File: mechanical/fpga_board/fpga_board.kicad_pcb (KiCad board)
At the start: 4 copper layers, 92 x 92 mm, 52 parts, among them J1 Conn_02x17_Odd_Even, J10 Conn_01x01, J2 Conn_02x17_Odd_Even, J3 Conn_02x17_Odd_Even, J4 Conn_02x17_Odd_Even, J5 Conn_02x17_Odd_Even, J6 jtag, J7 Conn_02x03_Odd_Even, J8 Conn_02x12_Odd_Even, J9 Conn_01x01, U1 XC6SLX16-FTG256, U2 SiT1602, U3 MIC5504-3.3YM5, U4 MIC5504-1.2YM5

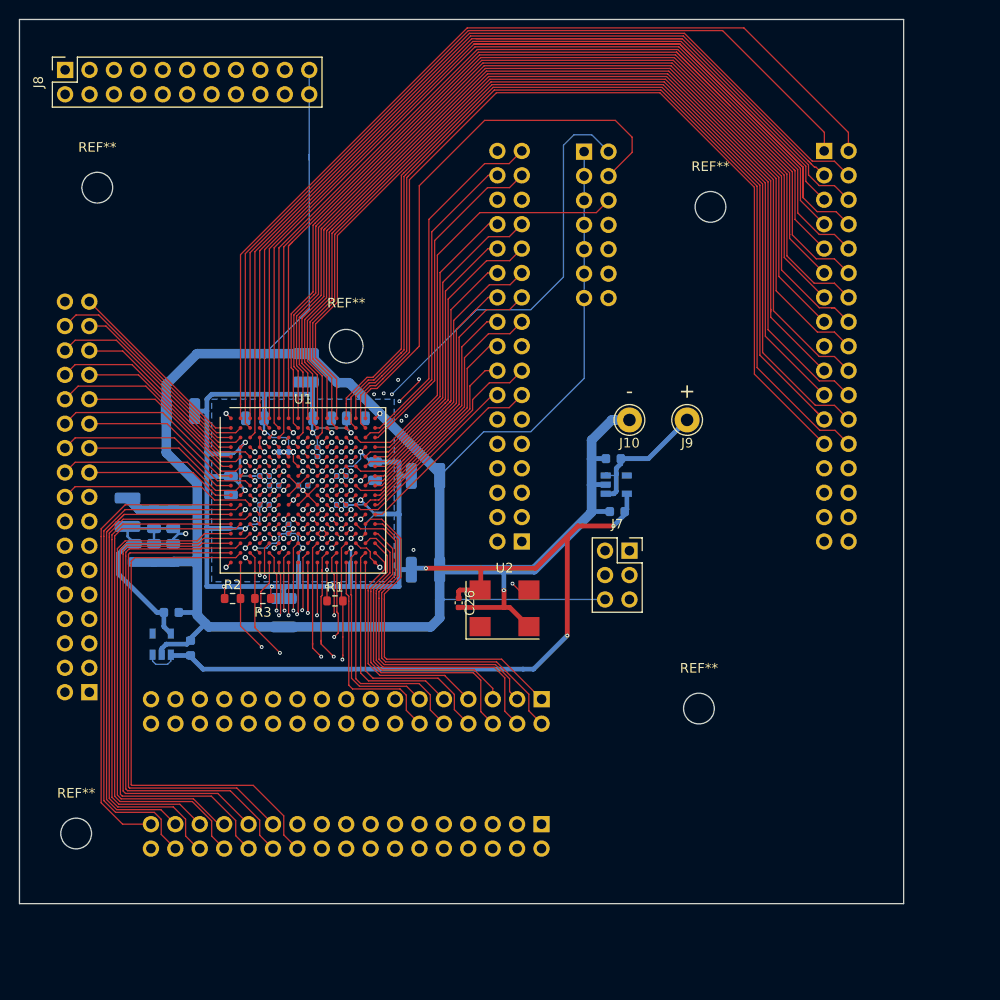
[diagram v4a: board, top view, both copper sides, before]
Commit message: Shortened some traces
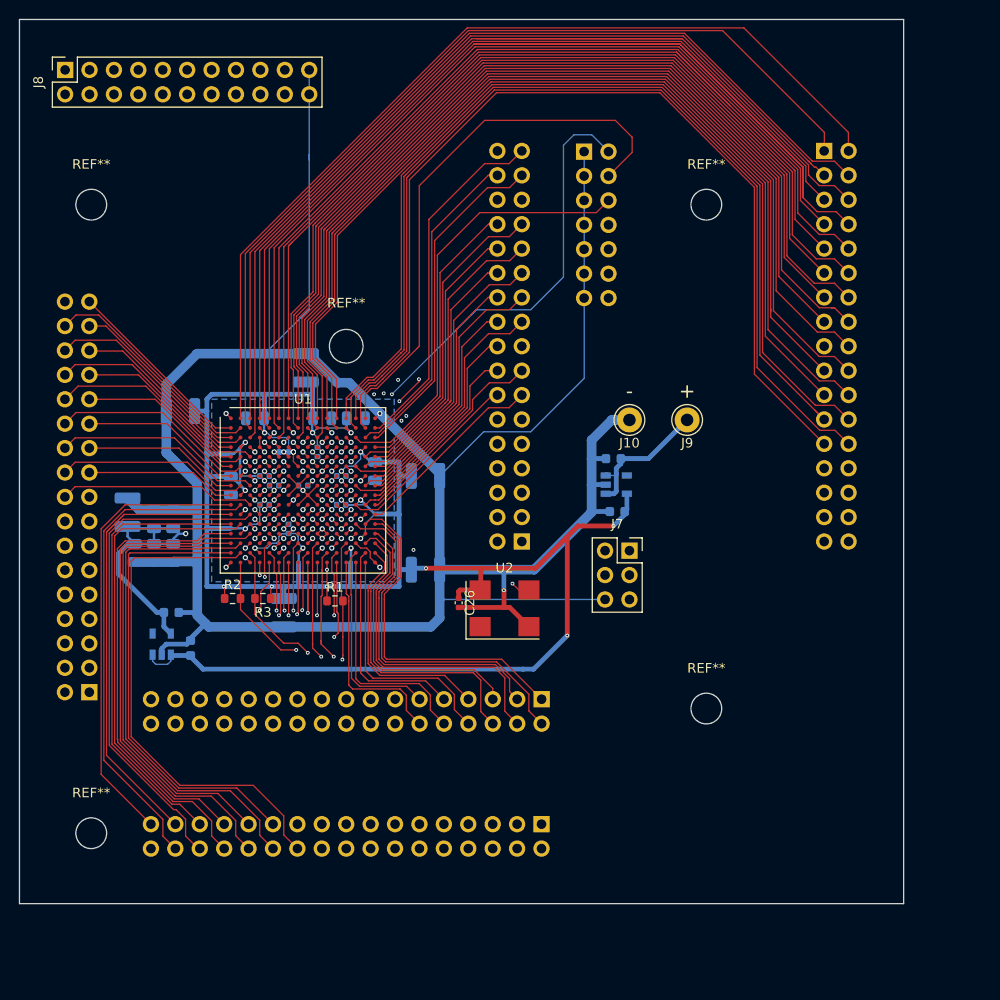
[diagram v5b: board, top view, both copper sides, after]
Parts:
- moved REF** 1.88 mm to (246.0, 174.0)
- moved REF** 1.57 mm to (246.0, 239.4)
- moved REF** 0.77 mm to (310.0, 226.4)
- moved REF** 0.49 mm to (310.0, 174.0)
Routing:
- net /T4-5: track 51.6 -> 29.0 mm
- net /T7-5: track 55.3 -> 32.7 mm
- net /T3-5: track 55.8 -> 33.5 mm
- net /T10+5: track 42.0 -> 20.0 mm
- net /T12+5: track 43.8 -> 23.0 mm
- net /T13+5: track 41.4 -> 20.9 mm
- net /T16+5: track 47.6 -> 27.2 mm
- net /T8-5: track 51.1 -> 30.7 mm
- net /T15+5: track 46.8 -> 27.2 mm
- net /T11+5: track 41.6 -> 22.3 mm
- net /T9+5: track 41.2 -> 22.0 mm
- net /T14+5: track 44.2 -> 25.2 mm
- net /T16-5: track 40.6 -> 22.7 mm
- net /T12-5: track 35.1 -> 19.4 mm
- net /T15-5: track 39.6 -> 25.5 mm
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
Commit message: drc fixes
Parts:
- moved C17 1.12 mm to (267.0, 199.2), turned to 0 degrees
- moved C18 0.98 mm to (266.0, 203.2), turned to 0 degrees
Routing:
- net /T9+5: track 22.0 -> 16.8 mm
- net /T12-5: track 19.4 -> 17.4 mm
- net /T15-5: track 25.5 -> 23.6 mm
- net /T10+5: track 20.0 -> 18.2 mm
- net /T16-5: track 22.7 -> 21.2 mm
- net /T13+5: track 20.9 -> 19.6 mm
- net /T1-4: track 69.3 -> 68.7 mm
- net /T11-5: track 20.9 -> 21.6 mm
- net /T5+4: track 95.0 -> 95.6 mm
